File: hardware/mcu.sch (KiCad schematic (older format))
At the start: 27 parts, among them P2 CONN_02X05, SW2 SW_PUSH, U11 TM4C1294KCPDT, Y1 NX5032GA

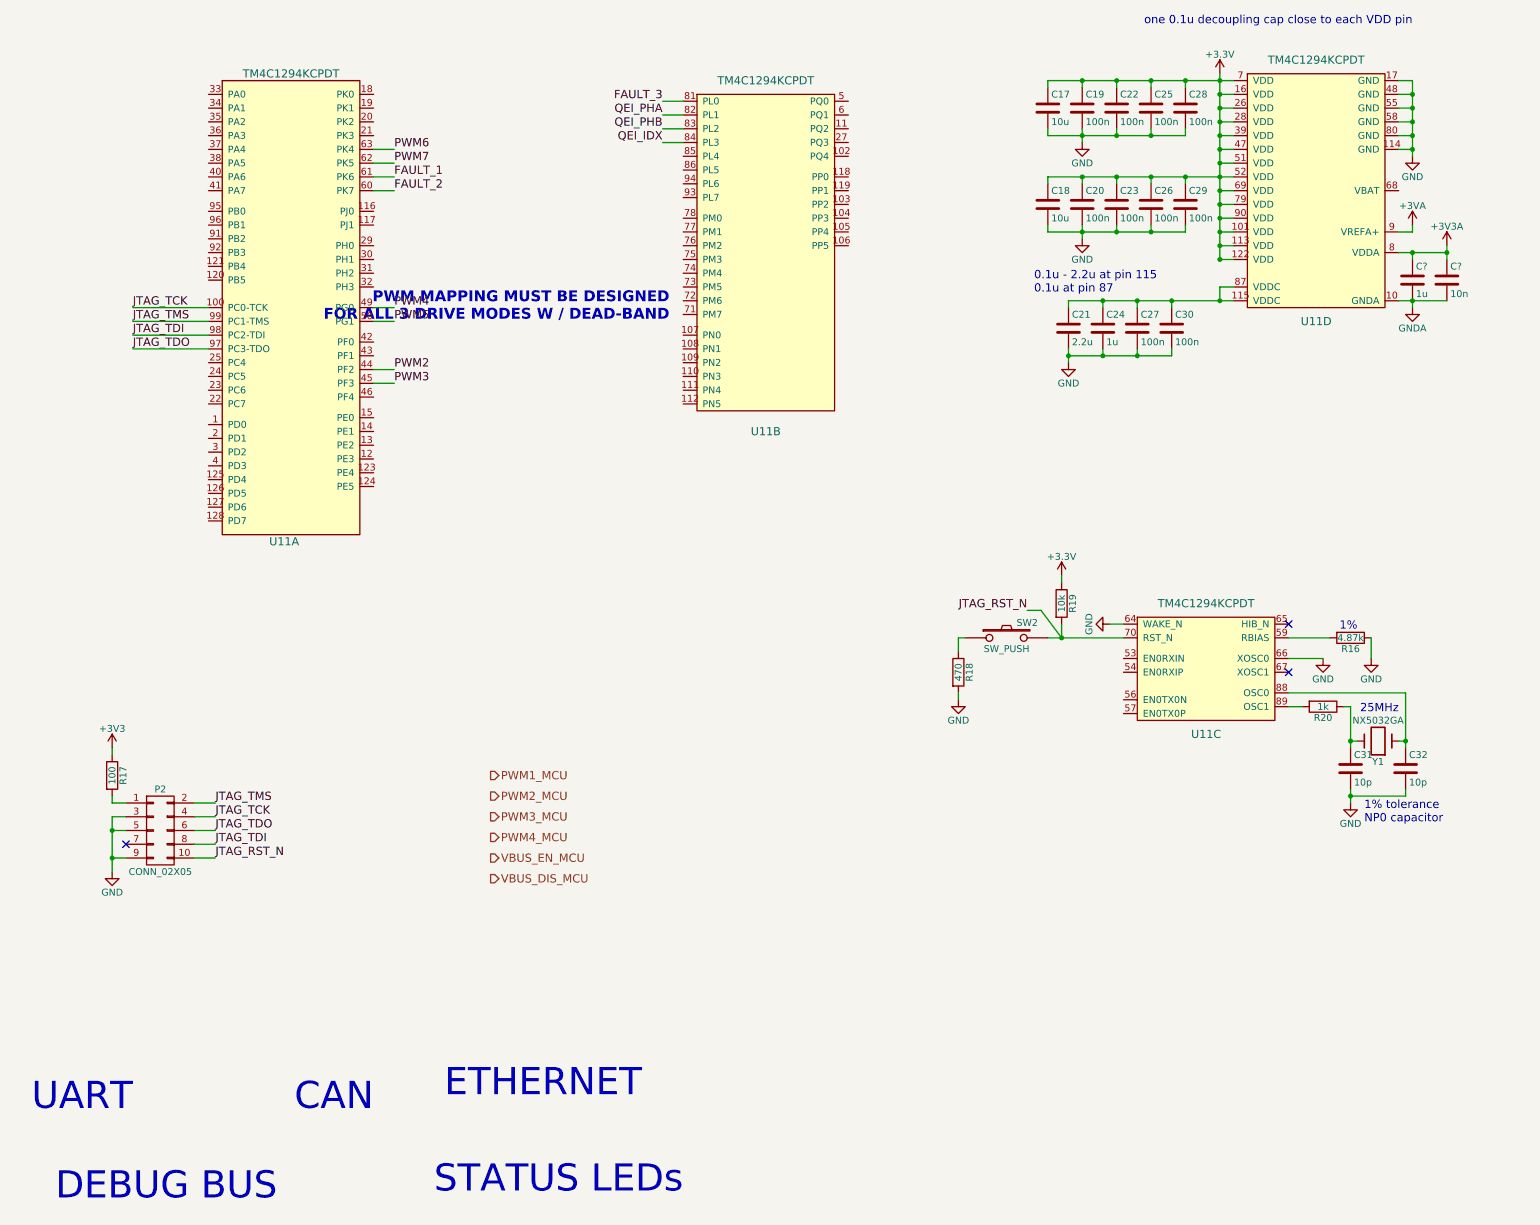
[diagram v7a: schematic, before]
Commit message: Finish MCU HW draft 1; adjust sensors for 3v ref
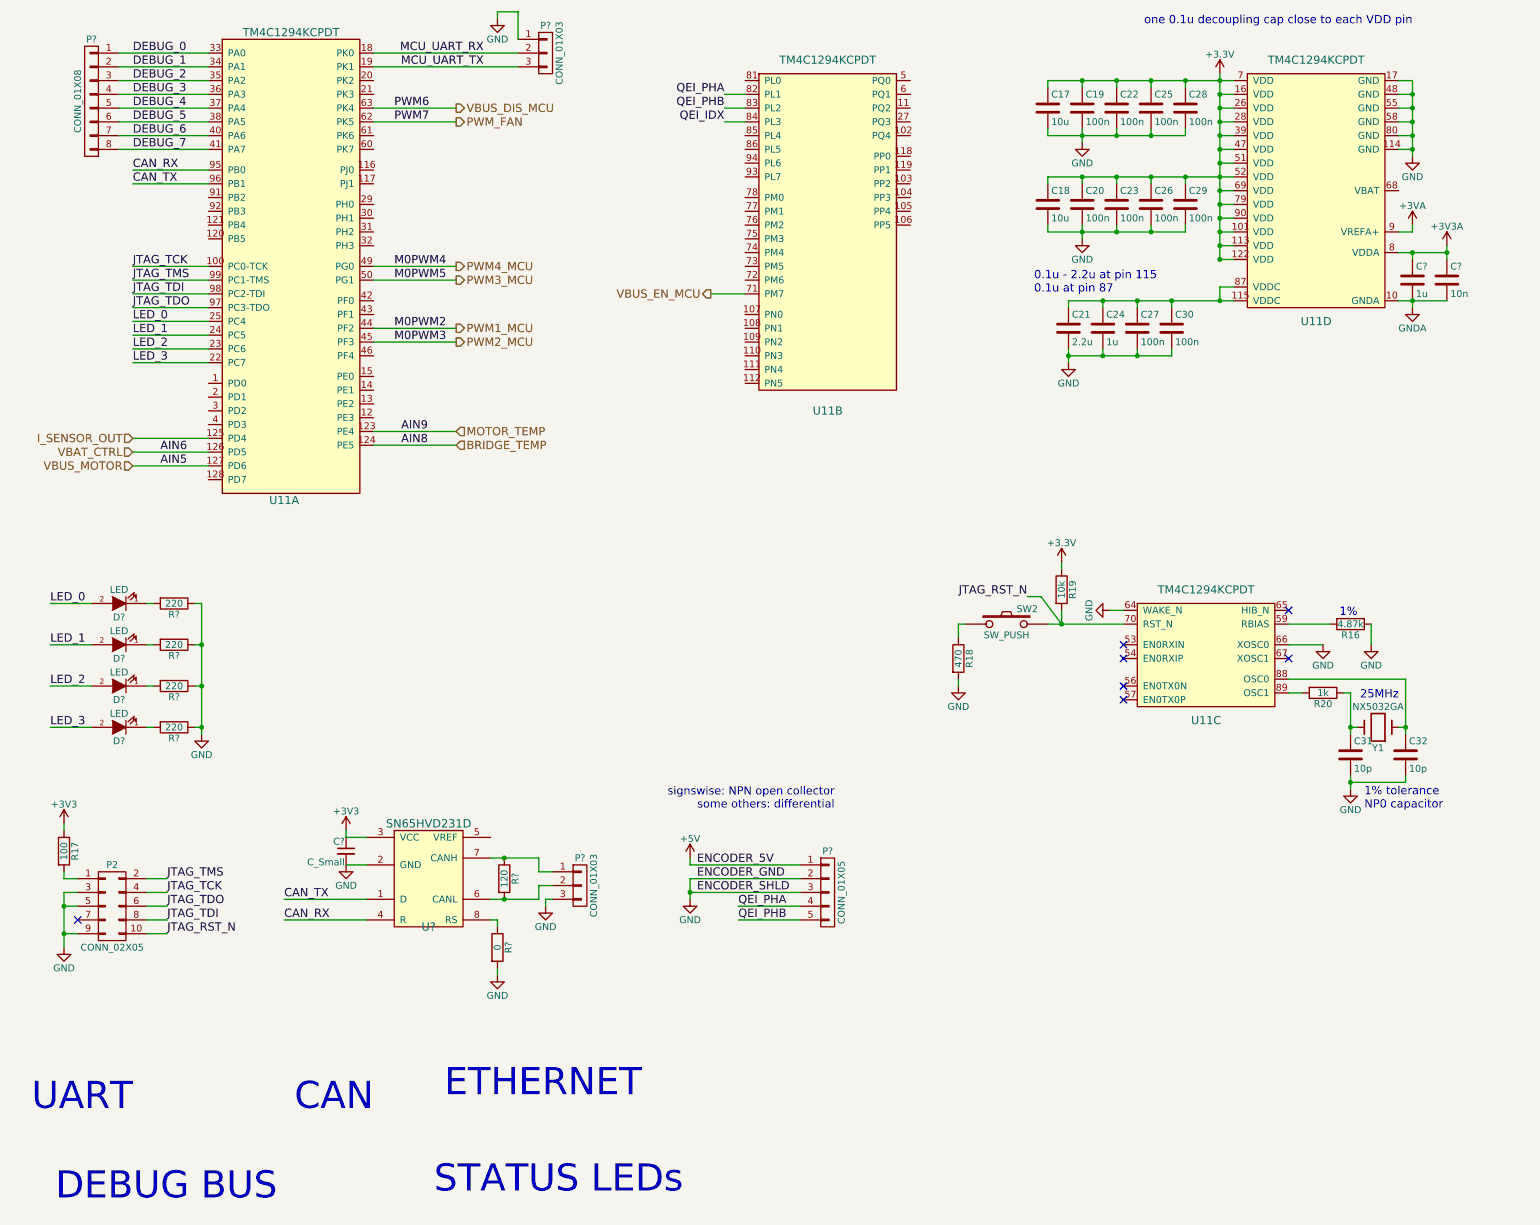
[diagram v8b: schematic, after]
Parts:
- added C?: C_Small, symbol C_Small
- added D? (x4): LED, symbol LED
- added P?: CONN_01X05, symbol CONN_01X05
- added P?: CONN_01X08, symbol CONN_01X08
- added P? (x2): CONN_01X03, symbol CONN_01X03
- added R?: 0, symbol R
- added R?: 120, symbol R
- added R? (x4): 220, symbol R
- added U?: SN65HVD231D, symbol SN65HVD231D
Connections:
- net PWM2 is gone; now on net PWM1_MCU: U11.44 (PF2)
- net PWM3 is gone; now on net PWM2_MCU: U11.45 (PF3)
- net PWM4 is gone; now on net PWM4_MCU: U11.49 (PG0)
- net PWM5 is gone; now on net PWM3_MCU: U11.50 (PG1)
- net PWM6 is gone; now on net VBUS_DIS_MCU: U11.63 (PK4)
- net +3V3: now also C?.1, U?.3 (VCC)
- net GND: now also C?.2, P?.1 (P1), P?.2 (P2), P?.3 (P3), P?.3 (P3), R?.1, R?.1, R?.1, R?.1, R?.2, U?.2 (GND)
- net QEI_PHA: now also P?.4 (P4)
- net QEI_PHB: now also P?.5 (P5)
- net VBUS_EN_MCU: now also U11.71 (PM7)
- net MOTOR_TEMP: now reaches U11.123 (PE4)
- net BRIDGE_TEMP: now reaches U11.124 (PE5)
- net I_SENSOR_OUT: now reaches U11.125 (PD4)
- net VBAT_CTRL: now reaches U11.126 (PD5)
- net VBUS_MOTOR: now reaches U11.127 (PD6)
- net MCU_UART_RX: now reaches U11.18 (PK0)
- net MCU_UART_RX: now also P?.2 (P2)
- net MCU_UART_TX: now reaches U11.19 (PK1)
- net MCU_UART_TX: now also P?.3 (P3)
- net LED_3: now reaches U11.22 (PC7)
- net LED_3: now also D?.2 (A)
- net LED_2: now reaches U11.23 (PC6)
- net LED_2: now also D?.2 (A)
- net LED_1: now reaches U11.24 (PC5)
- net LED_1: now also D?.2 (A)
- net LED_0: now reaches U11.25 (PC4)
- net LED_0: now also D?.2 (A)
- net DEBUG_0: now reaches U11.33 (PA0)
- net DEBUG_0: now also P?.1 (P1)
- net DEBUG_1: now reaches U11.34 (PA1)
- net DEBUG_1: now also P?.2 (P2)
- net DEBUG_2: now reaches U11.35 (PA2)
- net DEBUG_2: now also P?.3 (P3)
- net DEBUG_3: now reaches U11.36 (PA3)
- net DEBUG_3: now also P?.4 (P4)
- net DEBUG_4: now reaches U11.37 (PA4)
- net DEBUG_4: now also P?.5 (P5)
- net DEBUG_5: now reaches U11.38 (PA5)
- net DEBUG_5: now also P?.6 (P6)
- net DEBUG_6: now reaches U11.40 (PA6)
- net DEBUG_6: now also P?.7 (P7)
- net DEBUG_7: now reaches U11.41 (PA7)
- net DEBUG_7: now also P?.8 (P8)
- net CAN_RX: now reaches U11.95 (PB0)
- net CAN_RX: now also U?.4 (R)
- net CAN_TX: now reaches U11.96 (PB1)
- net CAN_TX: now also U?.1 (D)
- net FAULT_1: no longer names the net of U11.61 (PK6)
- net FAULT_2: no longer names the net of U11.60 (PK7)
- net FAULT_3: no longer names the net of U11.81 (PL0)
- net PWM7 renamed PWM_FAN
- new net: P?.2 (P2), R?.2, U?.6 (CANL)
- new net: P?.1 (P1), R?.1, U?.7 (CANH)
- new net: R?.1, U?.8 (RS)
- new net: D?.1 (K), R?.2 (x4)
- new net +5V: P?.1 (P1)
- no-connect marks 3 -> 7
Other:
- note added: "signswise: NPN open collector\nsome others: differential"
- note removed: "PWM MAPPING MUST BE DESIGNED\nFOR ALL 3 DRIVE MODES W / DEAD-BAND"
- moved on the sheet: C31, C32, P2, R16, R17, R18, R19, R20, SW2, U11A, U11B, U11C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
